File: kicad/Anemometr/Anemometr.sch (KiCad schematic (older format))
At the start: 155 parts, among them J1 TxD, J10 +Z1, J11 +Z2, J12 +Z3, J13 +Z4, J14 -Z1, J15 -Z2, J16 -Z3, J17 -Z4, J18 1 TxD+, J19 2 TxD-, J2 RxD, J20 3 RxD+, J21 4-5, J22 6 RxD-, J23 7-8, J24 Conn_01x01_Female, J3 TMP117, J4 TMP117, J5 RST, J6 TMP117, J7 TMP117, J8 SWD, J9 SWC, Q1 5N10, U1 STM32F103C8Tx, U2 TS5A3166DBVR, U3 TS5A3166DBVR, U4 TS5A3166DBVR, U5 TS5A3166DBVR, U6 NCP1117-3.3, U7 MCP1700-5, U8 LMV7239, U9 MCP1700-3.3, Y1 8MHz, Y2 25MHz

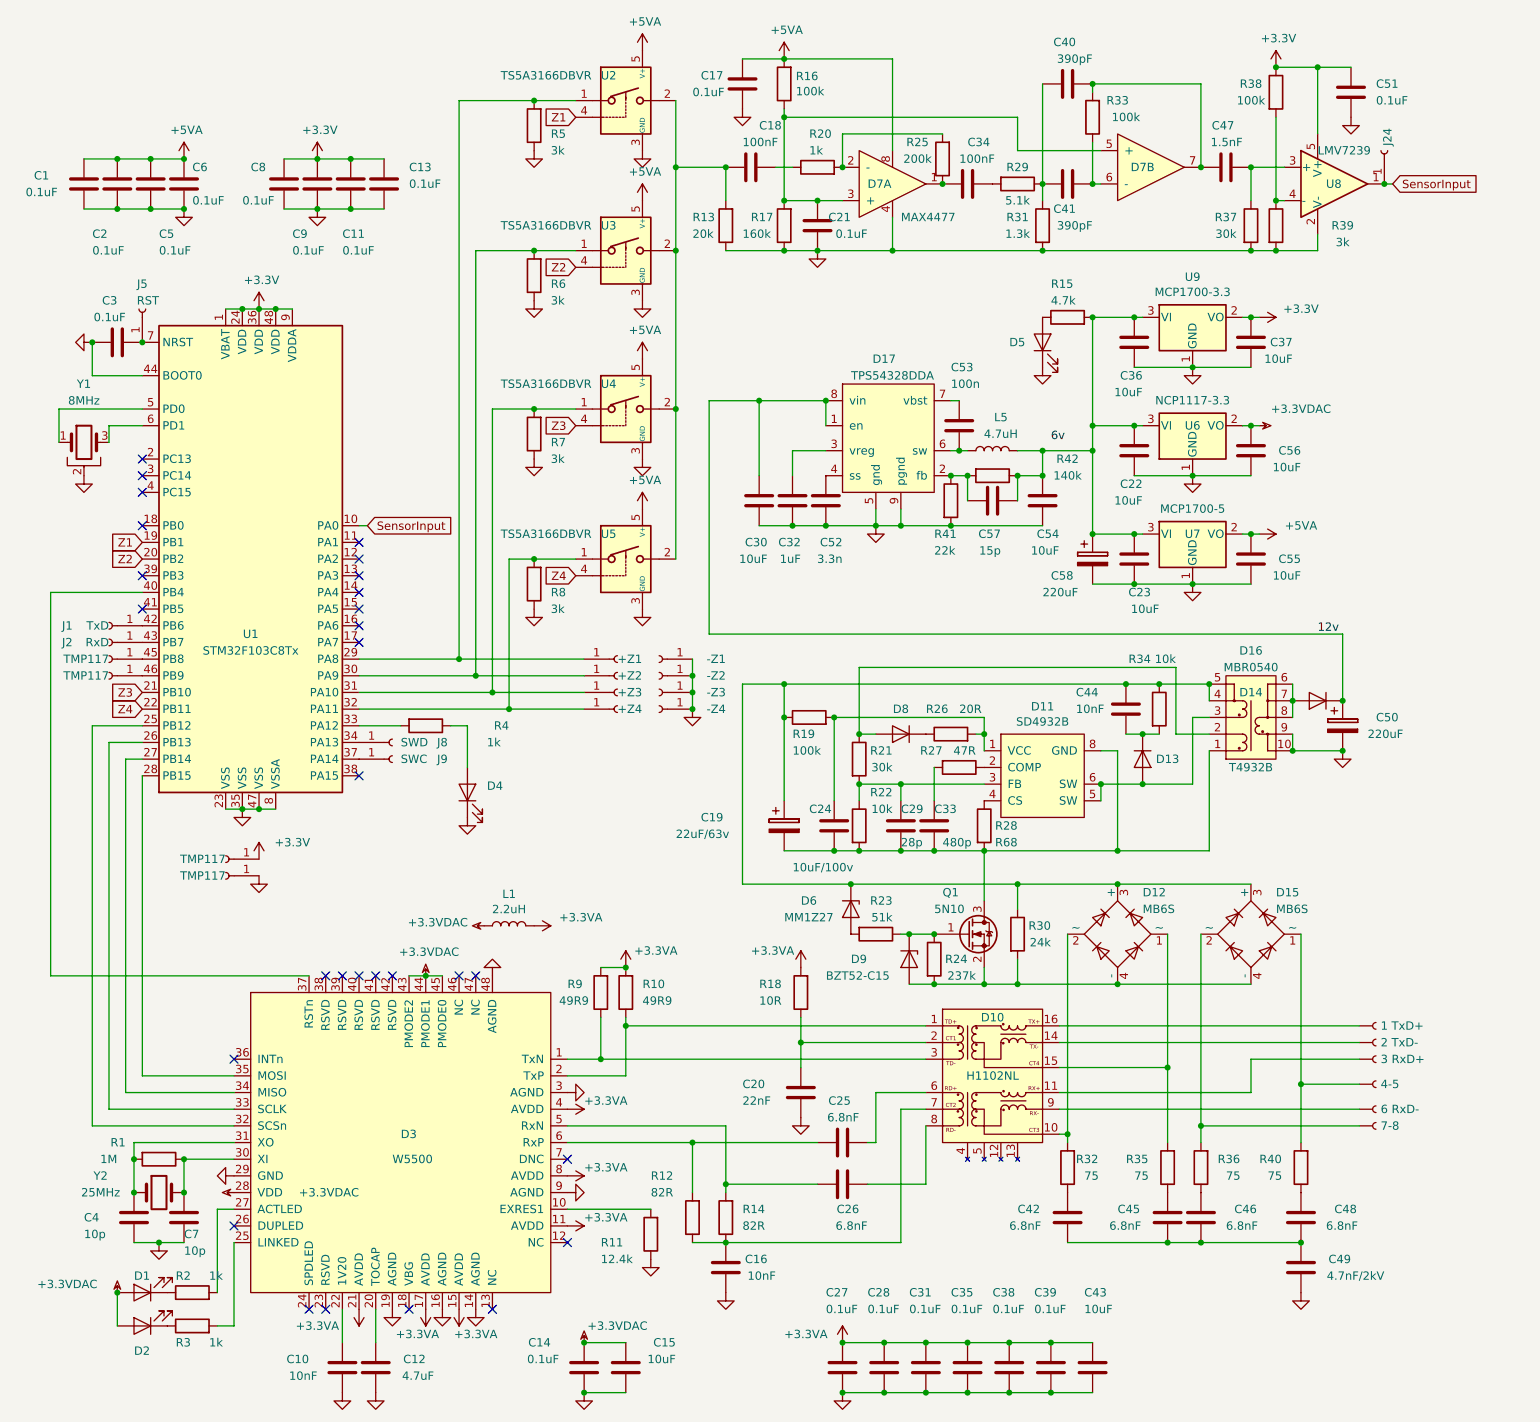
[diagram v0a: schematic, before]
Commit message: изменено:      kicad/Anemometr/Anemometr.sch 	изменено:      kicad/Anemometr/Anemometr.sch-bak
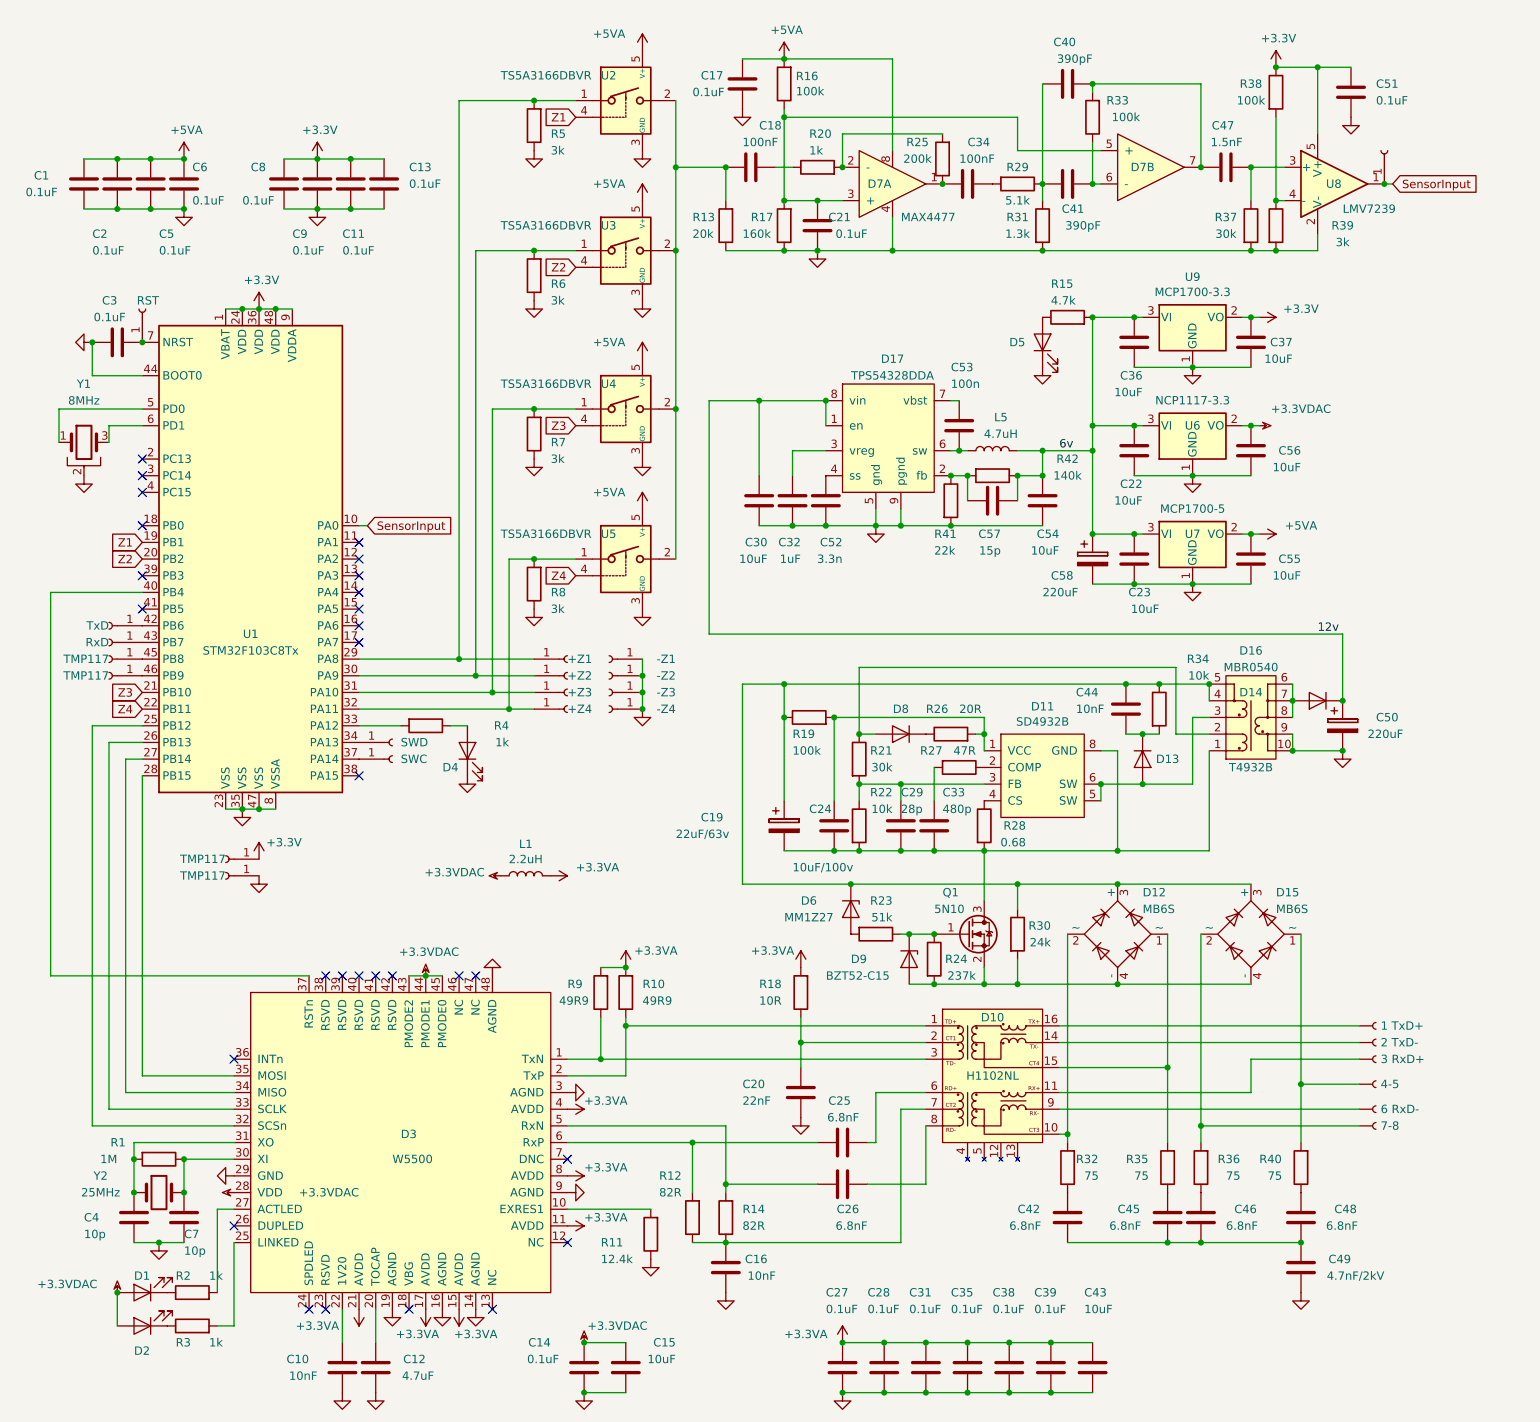
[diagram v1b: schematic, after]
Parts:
- R28: value R68 -> 0.68
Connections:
- net 6v: now also C22.2, C23.2, C36.2, C54.2, C57.2, C58.1, L5.2, R15.2, R42.1, U6.3 (VI), U7.3 (VI), U9.3 (VI)
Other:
- moved on the sheet: D4, L1

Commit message: изменено:      kicad/Anemometr/Anemometr.kicad_pcb 	изменено:      kicad/Anemometr/Anemometr.kicad_pcb-bak 	изменено:      kicad/Anemometr/Anemometr.sch 	изменено:      kicad/Anemometr/Anemometr.sch-bak 	изменено:      kicad/Anemometr/fp-info-cache
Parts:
- C54: value 10uF -> 22uF; footprint Capacitor_SMD:C_0805_2012Metric -> Capacitor_SMD:C_1210_3225Metric
- C58: value 220uF -> 1000uF
- D4, D5: footprint LED_SMD:LED_0805_2012Metric -> LED_SMD:LED_0603_1608Metric
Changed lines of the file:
@@
 U 1 1 61DF7EFE
 P 10400 4450
-F 0 "C23" H 10300 4650 50  0000 L CNN
-F 1 "10uF" H 10250 4750 50  0000 L CNN
+F 0 "C23" H 10250 4650 50  0000 L CNN
+F 1 "10uF" H 10200 4750 50  0000 L CNN
 F 2 "Capacitor_SMD:C_0805_2012Metric" H 10438 4300 50  0001 C CNN
 F 3 "~" H 10400 4450 50  0001 C CNN
@@
 F 0 "D4" V 6300 5750 50  0000 R CNN
 F 1 "LED" V 6348 5483 50  0001 R CNN
-F 2 "LED_SMD:LED_0805_2012Metric" H 6400 5600 50  0001 C CNN
+F 2 "LED_SMD:LED_0603_1608Metric" H 6400 5600 50  0001 C CNN
 F 3 "~" H 6400 5600 50  0001 C CNN
 	1    6400 5600
@@
 F 0 "D5" V 9850 3350 50  0000 R CNN
 F 1 "LED" V 9798 3033 50  0001 R CNN
-F 2 "LED_SMD:LED_0805_2012Metric" H 9850 3150 50  0001 C CNN
+F 2 "LED_SMD:LED_0603_1608Metric" H 9850 3150 50  0001 C CNN
 F 3 "~" H 9850 3150 50  0001 C CNN
 	1    9850 3150
@@
 U 1 1 62780B09
 P 9300 4100
-F 0 "R41" H 9200 3900 50  0000 L CNN
-F 1 "22k" H 9200 3800 50  0000 L CNN
+F 0 "R41" H 9200 3850 50  0000 L CNN
+F 1 "22k" H 9200 3750 50  0000 L CNN
 F 2 "Resistor_SMD:R_0603_1608Metric" V 9230 4100 50  0001 C CNN
 F 3 "~" H 9300 4100 50  0001 C CNN
@@
 U 1 1 62828535
 P 9850 4100
-F 0 "C54" H 9750 4300 50  0000 L CNN
-F 1 "10uF" H 9750 4400 50  0000 L CNN
-F 2 "Capacitor_SMD:C_0805_2012Metric" H 9888 3950 50  0001 C CNN
+F 0 "C54" H 9750 4350 50  0000 L CNN
+F 1 "22uF" H 9750 4450 50  0000 L CNN
+F 2 "Capacitor_SMD:C_1210_3225Metric" H 9888 3950 50  0001 C CNN
 F 3 "~" H 9850 4100 50  0001 C CNN
 	1    9850 4100
@@
 U 1 1 62C3F606
 P 9550 4100
-F 0 "C57" V 9350 4050 50  0000 L CNN
-F 1 "15p" V 9250 4050 50  0000 L CNN
+F 0 "C57" V 9300 4050 50  0000 L CNN
+F 1 "15p" V 9200 4050 50  0000 L CNN
 F 2 "Capacitor_SMD:C_0603_1608Metric" H 9588 3950 50  0001 C CNN
 F 3 "~" H 9550 4100 50  0001 C CNN
@@
 U 1 1 634D0174
 P 10150 4450
-F 0 "C58" H 9900 4350 50  0000 L CNN
-F 1 "220uF" H 9850 4250 50  0000 L CNN
+F 0 "C58" H 10050 4250 50  0000 L CNN
+F 1 "1000uF" H 10000 4150 50  0000 L CNN
 F 2 "Capacitor_Tantalum_SMD:CP_EIA-7343-15_Kemet-W" H 10188 4300 50  0001 C CNN
 F 3 "~" H 10150 4450 50  0001 C CNN

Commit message: изменено:      kicad/Anemometr/Anemometr.kicad_pcb 	изменено:      kicad/Anemometr/Anemometr.kicad_pcb-bak 	изменено:      kicad/Anemometr/Anemometr.sch 	изменено:      kicad/Anemometr/Anemometr.sch-bak 	изменено:      kicad/Anemometr/fp-info-cache
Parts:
- C24: value 10uF/100v -> 10uF
- C40, C41: value 390pF -> 390p
- L5: footprint Inductor_SMD:L_1812_4532Metric -> Inductor_SMD:L_Coilcraft_LPS4018
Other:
- moved on the sheet: C17, R16
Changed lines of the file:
@@
 L Device:R R16
 U 1 1 61CF7DC2
-P 8300 1600
-F 0 "R16" H 8230 1554 50  0000 R CNN
-F 1 "100k" H 8230 1645 50  0000 R CNN
-F 2 "Resistor_SMD:R_0603_1608Metric" V 8230 1600 50  0001 C CNN
-F 3 "~" H 8300 1600 50  0001 C CNN
-	1    8300 1600
+P 8300 1650
+F 0 "R16" H 8230 1604 50  0000 R CNN
+F 1 "100k" H 8230 1695 50  0000 R CNN
+F 2 "Resistor_SMD:R_0603_1608Metric" V 8230 1650 50  0001 C CNN
+F 3 "~" H 8300 1650 50  0001 C CNN
+	1    8300 1650
 	-1   0    0    1
 $EndComp
@@
 U 1 1 61CF8246
 P 8300 2450
-F 0 "R17" H 8500 2400 50  0000 R CNN
-F 1 "160k" H 8550 2500 50  0000 R CNN
+F 0 "R17" H 8500 2450 50  0000 R CNN
+F 1 "160k" H 8550 2550 50  0000 R CNN
 F 2 "Resistor_SMD:R_0603_1608Metric" V 8230 2450 50  0001 C CNN
 F 3 "~" H 8300 2450 50  0001 C CNN
@@
 U 1 1 61CF86C2
 P 9850 2450
-F 0 "R31" H 9700 2500 50  0000 C CNN
-F 1 "1.3k" H 9700 2400 50  0000 C CNN
+F 0 "R31" H 9700 2450 50  0000 C CNN
+F 1 "1.3k" H 9700 2350 50  0000 C CNN
 F 2 "Resistor_SMD:R_0603_1608Metric" V 9780 2450 50  0001 C CNN
 F 3 "~" H 9850 2450 50  0001 C CNN
@@
 U 1 1 61D227BC
 P 8100 2100
-F 0 "C18" V 7850 2150 50  0000 L CNN
-F 1 "100nF" V 7950 2050 50  0000 L CNN
+F 0 "C18" V 7950 1850 50  0000 L CNN
+F 1 "100nF" V 8050 1800 50  0000 L CNN
 F 2 "Capacitor_SMD:C_0603_1608Metric" H 8138 1950 50  0001 C CNN
 F 3 "~" H 8100 2100 50  0001 C CNN
@@
 U 1 1 61D240DB
 P 8500 2450
-F 0 "C21" H 8300 2400 50  0000 L CNN
-F 1 "0.1uF" H 8200 2500 50  0000 L CNN
+F 0 "C21" H 8250 2450 50  0000 L CNN
+F 1 "0.1uF" H 8200 2550 50  0000 L CNN
 F 2 "Capacitor_SMD:C_0603_1608Metric" H 8538 2300 50  0001 C CNN
 F 3 "~" H 8500 2450 50  0001 C CNN
@@
 U 1 1 61D25278
 P 7950 2450
-F 0 "R13" H 8150 2400 50  0000 R CNN
-F 1 "20k" H 8150 2500 50  0000 R CNN
+F 0 "R13" H 8150 2450 50  0000 R CNN
+F 1 "20k" H 8150 2550 50  0000 R CNN
 F 2 "Resistor_SMD:R_0603_1608Metric" V 7880 2450 50  0001 C CNN
 F 3 "~" H 7950 2450 50  0001 C CNN
@@
 U 1 1 61D32F05
 P 10000 1600
-F 0 "C40" V 10250 1550 50  0000 L CNN
-F 1 "390pF" V 10150 1450 50  0000 L CNN
+F 0 "C40" V 9850 1550 50  0000 L CNN
+F 1 "390p" V 9750 1500 50  0000 L CNN
 F 2 "Capacitor_SMD:C_0603_1608Metric" H 10038 1450 50  0001 C CNN
 F 3 "~" H 10000 1600 50  0001 C CNN
@@
 P 10000 2200
 F 0 "C41" V 9850 2100 50  0000 L CNN
-F 1 "390pF" V 9750 2000 50  0000 L CNN
+F 1 "390p" V 9750 2050 50  0000 L CNN
 F 2 "Capacitor_SMD:C_0603_1608Metric" H 10038 2050 50  0001 C CNN
 F 3 "~" H 10000 2200 50  0001 C CNN
@@
 P 10150 1800
 F 0 "R33" H 10000 1700 50  0000 C CNN
-F 1 "100k" H 9950 1800 50  0000 C CNN
+F 1 "100k" H 10000 1800 50  0000 C CNN
 F 2 "Resistor_SMD:R_0603_1608Metric" V 10080 1800 50  0001 C CNN
 F 3 "~" H 10150 1800 50  0001 C CNN
@@
 L Device:C C17
 U 1 1 61DD70B0
-P 8050 1600
-F 0 "C17" H 7800 1650 50  0000 L CNN
-F 1 "0.1uF" H 7750 1550 50  0000 L CNN
-F 2 "Capacitor_SMD:C_0603_1608Metric" H 8088 1450 50  0001 C CNN
-F 3 "~" H 8050 1600 50  0001 C CNN
-	1    8050 1600
+P 8050 1650
+F 0 "C17" H 7800 1700 50  0000 L CNN
+F 1 "0.1uF" H 7750 1600 50  0000 L CNN
+F 2 "Capacitor_SMD:C_0603_1608Metric" H 8088 1500 50  0001 C CNN
+F 3 "~" H 8050 1650 50  0001 C CNN
+	1    8050 1650
 	1    0    0    -1
 $EndComp
@@
 L power:GND #PWR052
 U 1 1 61DD78CC
-P 8050 1750
-F 0 "#PWR052" H 8050 1500 50  0001 C CNN
-F 1 "GND" H 8055 1577 50  0001 C CNN
-F 2 "" H 8050 1750 50  0001 C CNN
-F 3 "" H 8050 1750 50  0001 C CNN
-	1    8050 1750
+P 8050 1800
+F 0 "#PWR052" H 8050 1550 50  0001 C CNN
+F 1 "GND" H 8055 1627 50  0001 C CNN
+F 2 "" H 8050 1800 50  0001 C CNN
+F 3 "" H 8050 1800 50  0001 C CNN
+	1    8050 1800
 	1    0    0    -1
 $EndComp
@@
 U 1 1 61E0D55F
 P 9400 2200
-F 0 "C34" V 9150 2200 50  0000 L CNN
+F 0 "C34" V 9150 2150 50  0000 L CNN
 F 1 "100nF" V 9250 2150 50  0000 L CNN
 F 2 "Capacitor_SMD:C_0603_1608Metric" H 9438 2050 50  0001 C CNN
@@
 U 1 1 61D49242
 P 11100 2450
-F 0 "R37" H 10950 2500 50  0000 C CNN
-F 1 "30k" H 10950 2400 50  0000 C CNN
+F 0 "R37" H 10950 2450 50  0000 C CNN
+F 1 "30k" H 10950 2350 50  0000 C CNN
 F 2 "Resistor_SMD:R_0603_1608Metric" V 11030 2450 50  0001 C CNN
 F 3 "~" H 11100 2450 50  0001 C CNN
@@
 P 9000 2200
 F 0 "D7" H 8800 2200 50  0000 L CNN
-F 1 "MAX4477" H 9000 2000 50  0000 L CNN
+F 1 "MAX4477" H 9000 2050 50  0000 L CNN
 F 2 "Package_SO:MSOP-8_3x3mm_P0.65mm" H 9000 2200 50  0001 C CNN
 F 3 "" H 9000 2200 50  0001 C CNN
@@
 	8650 1900 9250 1900
 Connection ~ 8650 2100
-Wire Wire Line
-	8300 1750 8300 1800
 $Comp
 L MCU_ST_STM32F1:STM32F103C8Tx U1
@@
 U 1 1 629DA6BE
 P 8600 6050
-F 0 "C24" H 8450 6150 50  0000 L CNN
-F 1 "10uF/100v" H 8350 5800 50  0000 L CNN
+F 0 "C24" H 8400 6300 50  0000 L CNN
+F 1 "10uF" H 8400 6200 50  0000 L CNN
 F 2 "Capacitor_SMD:C_0805_2012Metric" H 8638 5900 50  0001 C CNN
 F 3 "~" H 8600 6050 50  0001 C CNN
@@
 L power:+5VA #PWR053
 U 1 1 61EE0C24
-P 8300 1450
-F 0 "#PWR053" H 8300 1300 50  0001 C CNN
-F 1 "+5VA" H 8315 1623 50  0000 C CNN
-F 2 "" H 8300 1450 50  0001 C CNN
-F 3 "" H 8300 1450 50  0001 C CNN
-	1    8300 1450
+P 8300 1500
+F 0 "#PWR053" H 8300 1350 50  0001 C CNN
+F 1 "+5VA" H 8315 1673 50  0000 C CNN
+F 2 "" H 8300 1500 50  0001 C CNN
+F 3 "" H 8300 1500 50  0001 C CNN
+	1    8300 1500
 	1    0    0    -1
 $EndComp
 Wire Wire Line
-	8050 1450 8300 1450
-Connection ~ 8300 1450
+	8050 1500 8300 1500
+Connection ~ 8300 1500
 Wire Wire Line
-	8300 1450 8950 1450
+	8300 1500 8950 1500
 Wire Wire Line
 	7000 7450 7200 7450
@@
 Connection ~ 10150 2200
 Wire Wire Line
-	8950 1450 8950 2000
-Wire Wire Line
 	8300 2300 8500 2300
 Connection ~ 8300 2300
@@
 U 1 1 62653016
 P 6800 4600
-F 0 "R8" H 6700 4650 50  0000 R CNN
-F 1 "3k" H 6700 4750 50  0000 R CNN
+F 0 "R8" H 6700 4700 50  0000 R CNN
+F 1 "3k" H 6700 4800 50  0000 R CNN
 F 2 "Resistor_SMD:R_0603_1608Metric" V 6730 4600 50  0001 C CNN
 F 3 "~" H 6800 4600 50  0001 C CNN
@@
 U 1 1 626559F5
 P 6800 3700
-F 0 "R7" H 6700 3750 50  0000 R CNN
-F 1 "3k" H 6700 3850 50  0000 R CNN
+F 0 "R7" H 6700 3800 50  0000 R CNN
+F 1 "3k" H 6700 3900 50  0000 R CNN
 F 2 "Resistor_SMD:R_0603_1608Metric" V 6730 3700 50  0001 C CNN
 F 3 "~" H 6800 3700 50  0001 C CNN
@@
 U 1 1 62658447
 P 6800 2750
-F 0 "R6" H 6700 2800 50  0000 R CNN
-F 1 "3k" H 6700 2900 50  0000 R CNN
+F 0 "R6" H 6700 2850 50  0000 R CNN
+F 1 "3k" H 6700 2950 50  0000 R CNN
 F 2 "Resistor_SMD:R_0603_1608Metric" V 6730 2750 50  0001 C CNN
 F 3 "~" H 6800 2750 50  0001 C CNN
@@
 U 1 1 6265ADD3
 P 6800 1850
-F 0 "R5" H 6700 1900 50  0000 R CNN
-F 1 "3k" H 6700 2000 50  0000 R CNN
+F 0 "R5" H 6700 1950 50  0000 R CNN
+F 1 "3k" H 6700 2050 50  0000 R CNN
 F 2 "Resistor_SMD:R_0603_1608Metric" V 6730 1850 50  0001 C CNN
 F 3 "~" H 6800 1850 50  0001 C CNN
@@
 Wire Wire Line
 	8300 1800 9700 1800
-Connection ~ 8300 1800
 Wire Wire Line
 	8300 1800 8300 2300
@@
 F 0 "L5" V 9750 3750 50  0000 C CNN
 F 1 "4.7uH" V 9650 3750 50  0000 C CNN
-F 2 "Inductor_SMD:L_1812_4532Metric" H 9550 3800 50  0001 C CNN
+F 2 "Inductor_SMD:L_Coilcraft_LPS4018" H 9550 3800 50  0001 C CNN
 F 3 "~" H 9550 3800 50  0001 C CNN
 	1    9550 3800
@@
 	6650 5350 6800 5350
 Connection ~ 6650 5350
+Connection ~ 8300 1800
+Wire Wire Line
+	8950 1500 8950 2000
 $EndSCHEMATC

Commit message: изменено:      kicad/Anemometr/Anemometr-cache.lib 	изменено:      kicad/Anemometr/Anemometr-rescue.lib 	изменено:      kicad/Anemometr/Anemometr.kicad_pcb 	изменено:      kicad/Anemometr/Anemometr.kicad_pcb-bak 	изменено:      kicad/Anemometr/Anemometr.sch 	изменено:      kicad/Anemometr/Anemometr.sch-bak
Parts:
- D17: symbol My_Library:TPS54328DDA -> Anemometr-rescue:TPS54328DDA-My_Library
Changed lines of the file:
@@
 $EndComp
 $Comp
-L My_Library:TPS54328DDA D17
+L Anemometr-rescue:TPS54328DDA-My_Library D17
 U 1 1 6272872B
 P 8950 3900

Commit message: изменено:      kicad/Anemometr/Anemometr.sch 	изменено:      kicad/Anemometr/Anemometr.sch-bak 	изменено:      stm32cubeide/Anemometer/Anemometer.ioc 	изменено:      stm32cubeide/Anemometer/Core/Inc/main.h 	изменено:      stm32cubeide/Anemometer/Core/Src/main.c 	изменено:      stm32cubeide/Anemometer/Core/Src/stm32f1xx_it.c 	изменено:      stm32cubeide/Anemometer/Release/Anemometer.bin 	изменено:      stm32cubeide/Anemometer/Release/Anemometer.elf 	изменено:      stm32cubeide/Anemometer/Release/Anemometer.list 	изменено:      stm32cubeide/Anemometer/Release/Anemometer.map 	изменено:      stm32cubeide/Anemometer/Release/Core/Src/main.o 	изменено:      stm32cubeide/Anemometer/Release/Core/Src/main.su 	изменено:      stm32cubeide/Anemometer/Release/Core/Src/stm32f1xx_it.o 	изменено:      stm32cubeide/Anemometer/Release/Core/Src/stm32f1xx_it.su
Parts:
- R17: value 160k -> 110k
- R25: value 200k -> 300k
- R39: value 3k -> 10k
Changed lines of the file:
@@
 P 9250 2050
 F 0 "R25" H 9400 1950 50  0000 C CNN
-F 1 "200k" H 9400 2050 50  0000 C CNN
+F 1 "300k" H 9400 2050 50  0000 C CNN
 F 2 "Resistor_SMD:R_0603_1608Metric" V 9180 2050 50  0001 C CNN
 F 3 "~" H 9250 2050 50  0001 C CNN
@@
 P 8300 2450
 F 0 "R17" H 8500 2450 50  0000 R CNN
-F 1 "160k" H 8550 2550 50  0000 R CNN
+F 1 "110k" H 8550 2550 50  0000 R CNN
 F 2 "Resistor_SMD:R_0603_1608Metric" V 8230 2450 50  0001 C CNN
 F 3 "~" H 8300 2450 50  0001 C CNN
@@
 P 11250 2450
 F 0 "R39" H 11650 2450 50  0000 C CNN
-F 1 "3k" H 11650 2350 50  0000 C CNN
+F 1 "10k" H 11650 2350 50  0000 C CNN
 F 2 "Resistor_SMD:R_0603_1608Metric" V 11180 2450 50  0001 C CNN
 F 3 "~" H 11250 2450 50  0001 C CNN
